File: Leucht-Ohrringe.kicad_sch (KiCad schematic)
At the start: 18 parts, among them J1 Conn_ARM_SWD_TagConnect_TC2030, P1 USB_C_Plug_USB2.0, U4 CH340N, U5 nRF52832-QFxx

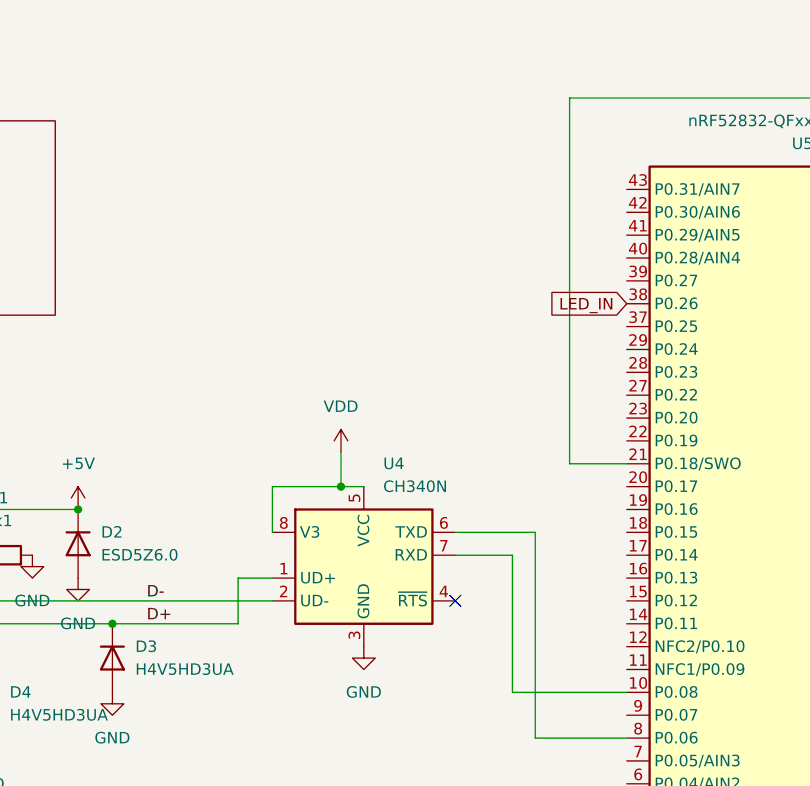
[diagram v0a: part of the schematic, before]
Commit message: add 6-axis imu
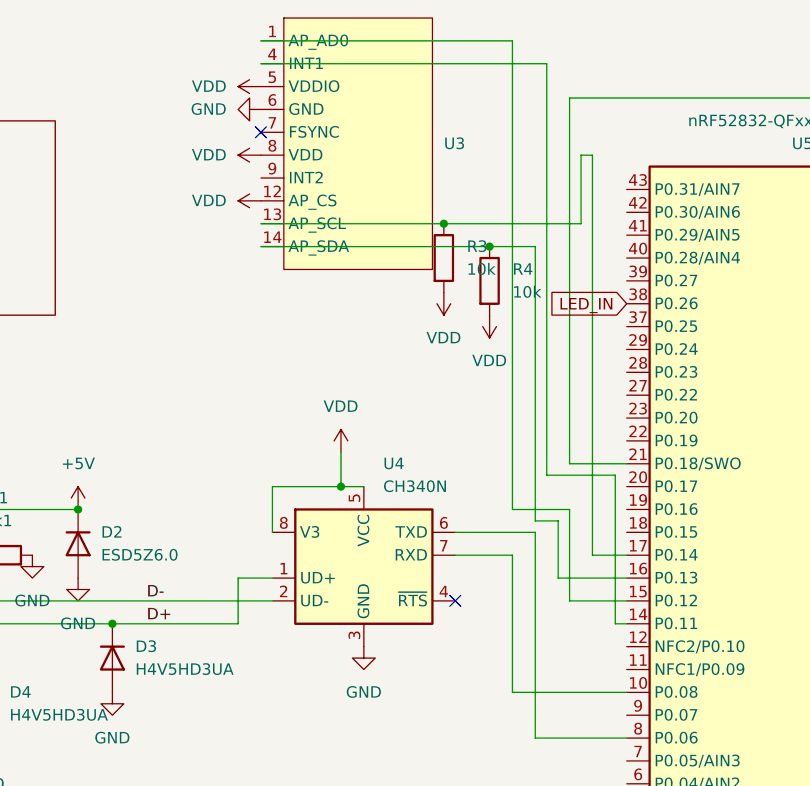
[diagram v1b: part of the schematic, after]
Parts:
- added R3, R4: 10k, Resistor_SMD:R_0402_1005Metric_Pad0.72x0.64mm_HandSolder, symbol Device:R
- added U3: (no value), Package_LGA:Bosch_LGA-14_3x2.5mm_P0.5mm, symbol custom:ICM_42670-L
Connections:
- net GND: now also U3.6 (GND)
- net VDD: now also R3.2, R4.2, U3.12 (AP_CS), U3.5 (VDDIO), U3.8 (VDD)
- net at U5.14 (P0.11): now also U3.4 (INT1)
- net at U5.15 (P0.12): now also U3.1 (AP_AD0)
- net at U5.16 (P0.13): now also R4.1, U3.14 (AP_SDA)
- net at U5.17 (P0.14): now also R3.1, U3.13 (AP_SCL)
- no-connect marks 4 -> 5

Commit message: move usb closer to the edge, add ntc
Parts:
- added R5: 100k, Resistor_SMD:R_0402_1005Metric_Pad0.72x0.64mm_HandSolder, symbol Device:R
- added TH1: Thermistor_NTC, Resistor_SMD:R_0402_1005Metric_Pad0.72x0.64mm_HandSolder, symbol Device:Thermistor_NTC
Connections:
- net +5V: now also J1.1 (VCC)
- net GND: now also TH1.2
- net VDD: now also R5.1
- net at U5.12 (NFC2/P0.10): now also R5.2, TH1.1
- no-connect marks 5 -> 4

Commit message: switch some components to jlc basic parts
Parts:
- C1: footprint Capacitor_SMD:C_0201_0603Metric -> Capacitor_SMD:C_0805_2012Metric; LCSC (none) -> C52923
- C2: footprint Capacitor_SMD:C_0201_0603Metric -> Capacitor_SMD:C_0402_1005Metric; LCSC (none) -> C1546
- C3: footprint Capacitor_SMD:C_0201_0603Metric -> Capacitor_SMD:C_0402_1005Metric; LCSC (none) -> C1525
- C4: LCSC (none) -> C17168
- L1: value 0 -> 6,8nH; footprint Capacitor_SMD:C_0402_1005Metric -> Inductor_SMD:L_0402_1005Metric; LCSC (none) -> C77110
- P1: LCSC (none) -> C668623
- R1: LCSC (none) -> C2907044
- R2: footprint Capacitor_SMD:C_0402_1005Metric -> Resistor_SMD:R_0402_1005Metric; LCSC (none) -> C17168
- R3, R4, TH1: LCSC (none) -> C49247682
- R5: LCSC (none) -> C25741
- U1, U2: value (none) -> TX4204; LCSC (none) -> C5122342
- U3: value (none) -> ICM-42670-L; LCSC (none) -> C49073546
- U4: LCSC (none) -> C2977777
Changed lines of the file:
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@@
 			)
 		)
+		(property "LCSC" "C668623"
+			(at 55.88 85.09 0)
+			(hide yes)
+			(show_name no)
+			(do_not_autoplace no)
+			(effects
+				(font
+					(size 1.27 1.27)
+				)
+			)
+		)
 		(pin "B5"
 		)
@@
 			)
 		)
-		(property "Value" "0"
+		(property "Value" "6,8nH"
 			(at 201.93 87.63 90)
 			(show_name no)
@@
 			)
 		)
-		(property "Footprint" "Capacitor_SMD:C_0402_1005Metric"
+		(property "Footprint" "Inductor_SMD:L_0402_1005Metric"
 			(at 201.93 90.17 0)
 			(hide yes)
@@
 			)
 		)
+		(property "LCSC" "C77110"
+			(at 201.93 90.17 90)
+			(hide yes)
+			(show_name no)
+			(do_not_autoplace no)
+			(effects
+				(font
+					(size 1.27 1.27)
+				)
+			)
+		)
 		(pin "2"
 		)
@@
 			)
 		)
-		(property "Footprint" "Capacitor_SMD:C_0201_0603Metric"
+		(property "Footprint" "Capacitor_SMD:C_0402_1005Metric"
 			(at 176.2252 146.05 0)
 			(hide yes)
@@
 			)
 		)
+		(property "LCSC" "C1546"
+			(at 175.26 142.24 0)
+			(hide yes)
+			(show_name no)
+			(do_not_autoplace no)
+			(effects
+				(font
+					(size 1.27 1.27)
+				)
+			)
+		)
 		(pin "2"
 		)
@@
 			)
 		)
+		(property "LCSC" "C49247682"
+			(at 124.46 99.06 0)
+			(hide yes)
+			(show_name no)
+			(do_not_autoplace no)
+			(effects
+				(font
+					(size 1.27 1.27)
+				)
+			)
+		)
 		(pin "1"
 		)
@@
 			)
 		)
-		(property "Footprint" "Capacitor_SMD:C_0201_0603Metric"
+		(property "Footprint" "Capacitor_SMD:C_0402_1005Metric"
 			(at 181.3052 123.19 0)
 			(hide yes)
@@
 			)
 		)
+		(property "LCSC" "C1525"
+			(at 180.34 119.38 0)
+			(hide yes)
+			(show_name no)
+			(do_not_autoplace no)
+			(effects
+				(font
+					(size 1.27 1.27)
+				)
+			)
+		)
 		(pin "2"
 		)
@@
 			)
 		)
+		(property "LCSC" "C17168"
+			(at 194.31 90.17 90)
+			(hide yes)
+			(show_name no)
+			(do_not_autoplace no)
+			(effects
+				(font
+					(size 1.27 1.27)
+				)
+			)
+		)
 		(pin "2"
 		)
@@
 			)
 		)
+		(property "LCSC" "C2907044"
+			(at 74.93 74.93 90)
+			(hide yes)
+			(show_name no)
+			(do_not_autoplace no)
+			(effects
+				(font
+					(size 1.27 1.27)
+				)
+			)
+		)
 		(pin "2"
 		)
@@
 			)
 		)
-		(property "Footprint" "Capacitor_SMD:C_0201_0603Metric"
+		(property "Footprint" "Capacitor_SMD:C_0805_2012Metric"
 			(at 171.1452 133.35 0)
 			(hide yes)
@@
 			)
 		)
+		(property "LCSC" "C52923"
+			(at 170.18 129.54 0)
+			(hide yes)
+			(show_name no)
+			(do_not_autoplace no)
+			(effects
+				(font
+					(size 1.27 1.27)
+				)
+			)
+		)
 		(pin "2"
 		)
@@
 			)
 		)
-		(property "Value" ""
+		(property "Value" "TX4204"
 			(at 129.54 121.92 0)
 			(show_name no)
@@
 			)
 		)
+		(property "LCSC" "C5122342"
+			(at 129.54 121.92 0)
+			(hide yes)
+			(show_name no)
+			(do_not_autoplace no)
+			(effects
+				(font
+					(size 1.27 1.27)
+				)
+			)
+		)
 		(pin "3"
 		)
@@
 			)
 		)
-		(property "Value" ""
+		(property "Value" "ICM-42670-L"
 			(at 107.95 44.45 0)
 			(show_name no)
@@
 			)
 		)
+		(property "LCSC" "C49073546"
+			(at 107.95 44.45 0)
+			(hide yes)
+			(show_name no)
+			(do_not_autoplace no)
+			(effects
+				(font
+					(size 1.27 1.27)
+				)
+			)
+		)
 		(pin "5"
 		)
@@
 			)
 		)
+		(property "LCSC" "C49247682"
+			(at 129.54 44.45 0)
+			(hide yes)
+			(show_name no)
+			(do_not_autoplace no)
+			(effects
+				(font
+					(size 1.27 1.27)
+				)
+			)
+		)
 		(pin "1"
 		)
@@
 			)
 		)
+		(property "LCSC" "C25741"
+			(at 124.46 91.44 0)
+			(hide yes)
+			(show_name no)
+			(do_not_autoplace no)
+			(effects
+				(font
+					(size 1.27 1.27)
+				)
+			)
+		)
 		(pin "1"
 		)
@@
 			)
 		)
+		(property "LCSC" "C2977777"
+			(at 115.57 74.93 0)
+			(hide yes)
+			(show_name no)
+			(do_not_autoplace no)
+			(effects
+				(font
+					(size 1.27 1.27)
+				)
+			)
+		)
 		(pin "1"
 		)
@@
 			)
 		)
-		(property "Footprint" "Capacitor_SMD:C_0402_1005Metric"
+		(property "Footprint" "Resistor_SMD:R_0402_1005Metric"
 			(at 199.898 93.98 90)
 			(hide yes)
@@
 			)
 		)
+		(property "LCSC" "C17168"
+			(at 198.12 93.98 0)
+			(hide yes)
+			(show_name no)
+			(do_not_autoplace no)
+			(effects
+				(font
+					(size 1.27 1.27)
+				)
+			)
+		)
 		(pin "1"
 		)
@@
 			)
 		)
-		(property "Value" ""
+		(property "Value" "TX4204"
 			(at 83.82 104.14 0)
 			(show_name no)
@@
 			)
 		)
+		(property "LCSC" "C5122342"
+			(at 83.82 104.14 0)
+			(hide yes)
+			(show_name no)
+			(do_not_autoplace no)
+			(effects
+				(font
+					(size 1.27 1.27)
+				)
+			)
+		)
 		(pin "3"
 		)
@@
 			(at 124.46 41.91 0)
 			(hide yes)
+			(show_name no)
+			(do_not_autoplace no)
+			(effects
+				(font
+					(size 1.27 1.27)
+				)
+			)
+		)
+		(property "LCSC" "C49247682"
+			(at 124.46 41.91 0)
+			(hide yes)

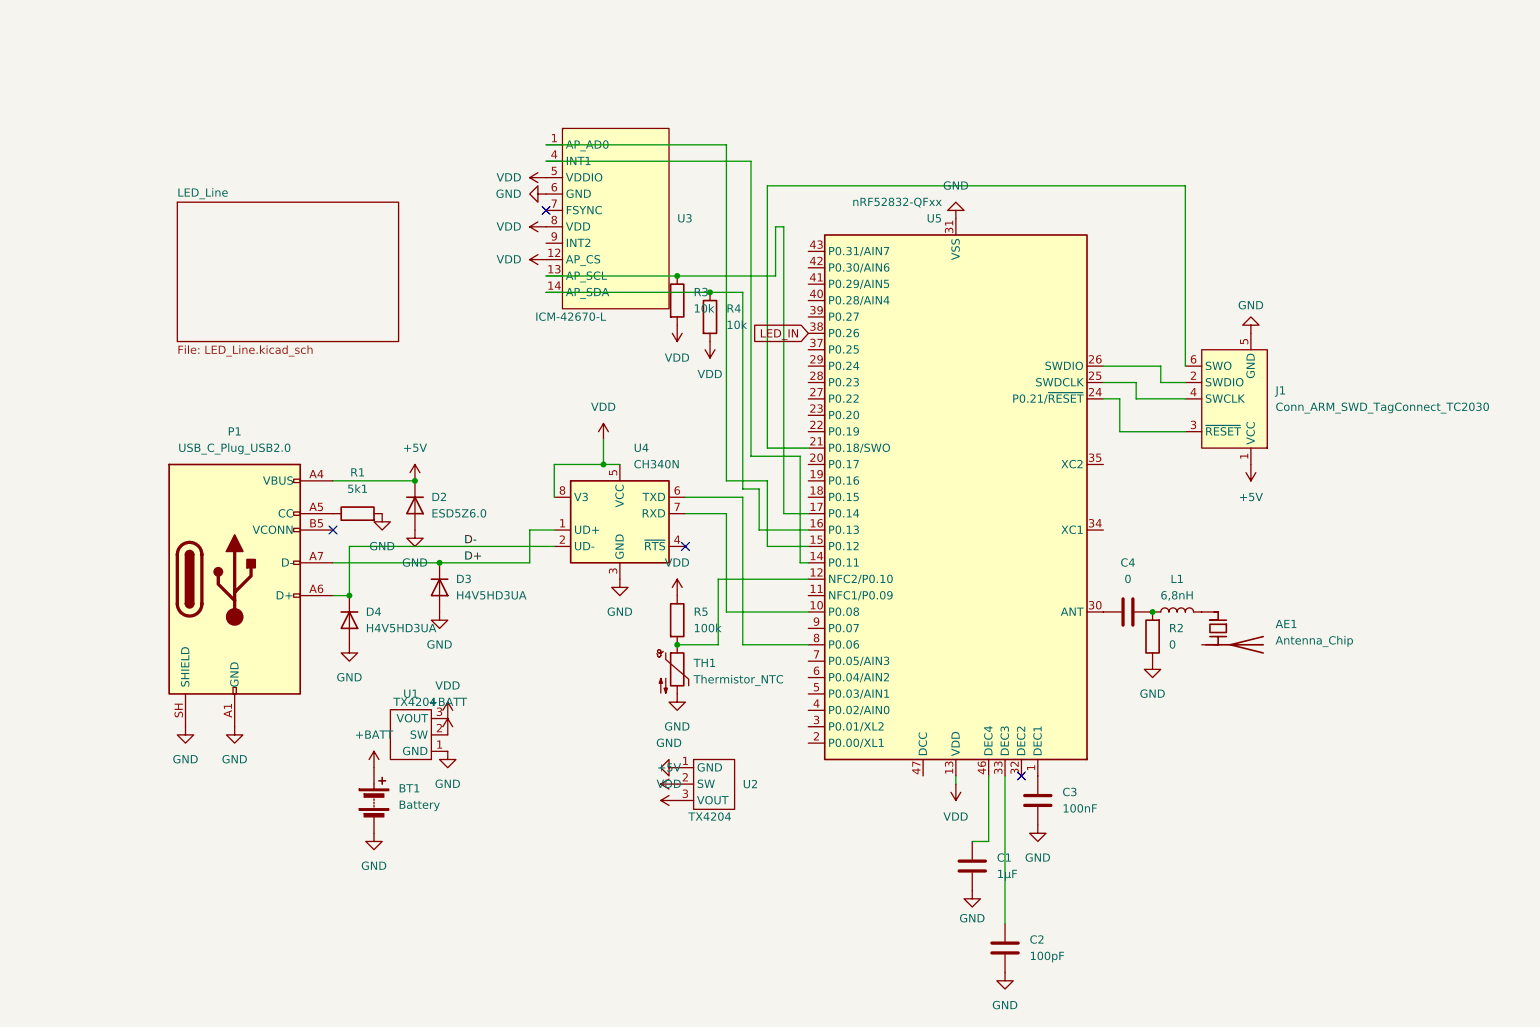
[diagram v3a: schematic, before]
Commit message: add decoupling caps for icm imu, select smaller footrpint for cap
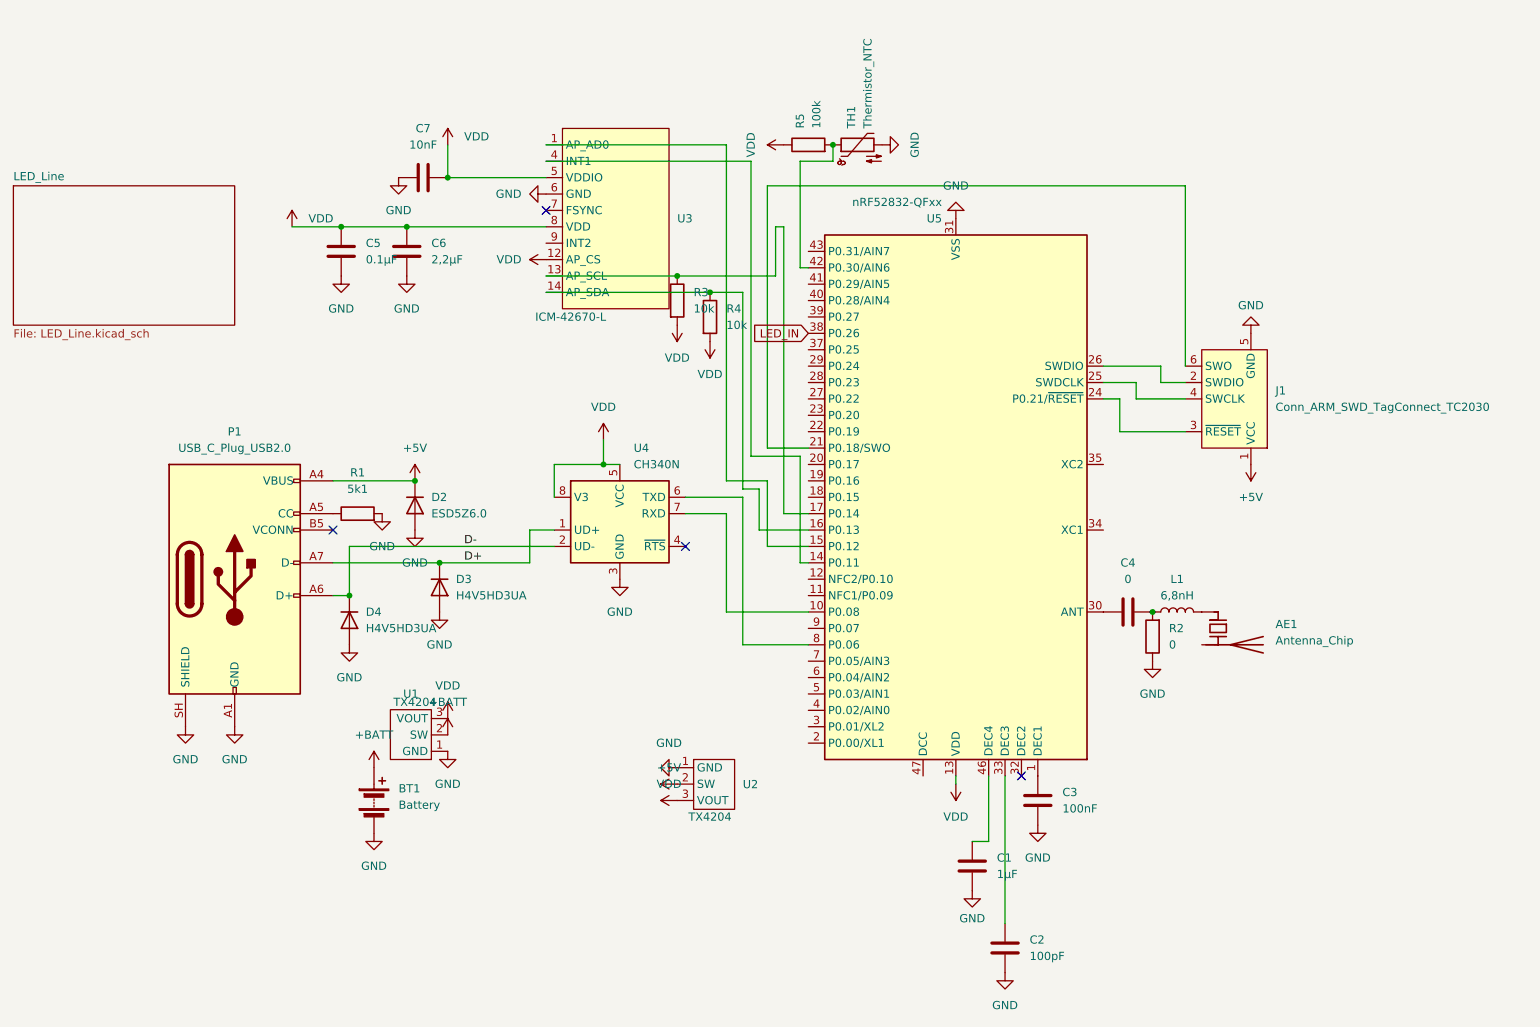
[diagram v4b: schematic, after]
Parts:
- added C5: 0.1µF, Capacitor_SMD:C_0402_1005Metric_Pad0.74x0.62mm_HandSolder, symbol Device:C
- added C6: 2,2µF, Capacitor_SMD:C_0402_1005Metric_Pad0.74x0.62mm_HandSolder, symbol Device:C
- added C7: 10nF, Capacitor_SMD:C_0402_1005Metric_Pad0.74x0.62mm_HandSolder, symbol Device:C
- C1: footprint Capacitor_SMD:C_0805_2012Metric -> Capacitor_SMD:C_0402_1005Metric
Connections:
- net GND: now also C5.1, C6.2, C7.1
- net VDD: now also C5.2, C6.1, C7.2
- net at R5.2, TH1.1: now also U5.42 (P0.30/AIN6); no longer U5.12 (NFC2/P0.10)
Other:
- moved on the sheet: R5, TH1

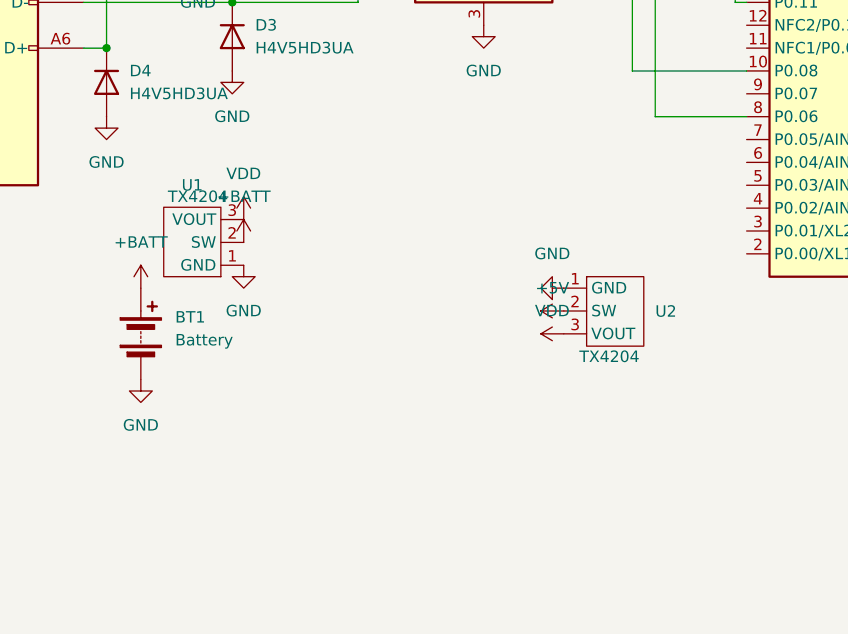
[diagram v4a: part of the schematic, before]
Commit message: fix buck converter circuit, add switch for 5V usb/off/swd power and bat power
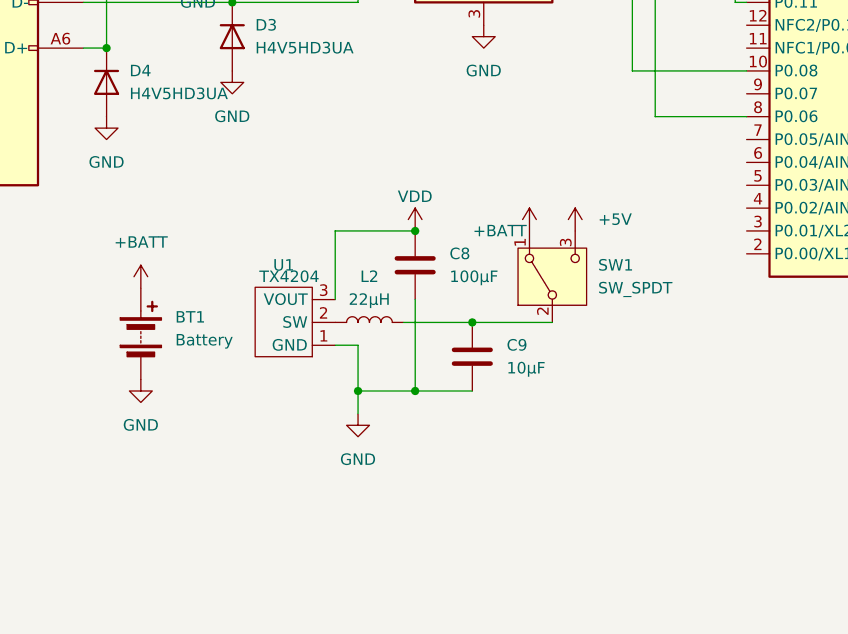
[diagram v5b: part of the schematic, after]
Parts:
- removed U2: TX4204, Package_TO_SOT_SMD:SOT-23-3, symbol custom:TX4204
- added C8: 100µF, Capacitor_SMD:C_1206_3216Metric_Pad1.33x1.80mm_HandSolder, symbol Device:C
- added C9: 10µF, Capacitor_SMD:C_0603_1608Metric_Pad1.08x0.95mm_HandSolder, symbol Device:C
- added L2: 22µH, Inductor_SMD:FNR3015S, symbol Device:L
- added SW1: SW_SPDT, Inductor_SMD:K3-1236S, symbol Switch:SW_SPDT
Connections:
- net +5V: now also SW1.3 (C)
- net +BATT: now also SW1.1 (A); no longer U1.2 (SW)
- net GND: now also C8.2, C9.2
- net VDD: now also C8.1
- new net: C9.1, L2.2, SW1.2 (B)
- new net: L2.1, U1.2 (SW)
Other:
- moved on the sheet: U1
